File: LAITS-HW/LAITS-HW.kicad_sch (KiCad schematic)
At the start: 0 parts

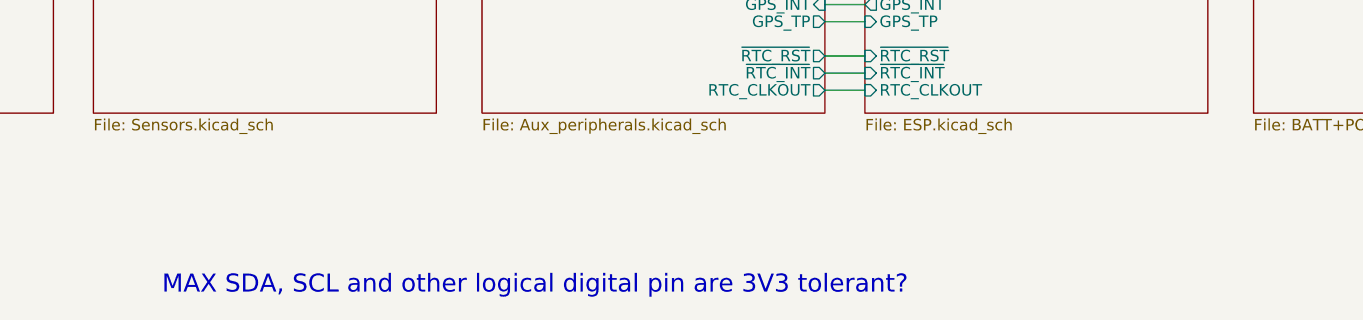
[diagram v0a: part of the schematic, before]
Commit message: improved silkscreen placement and some minor changes
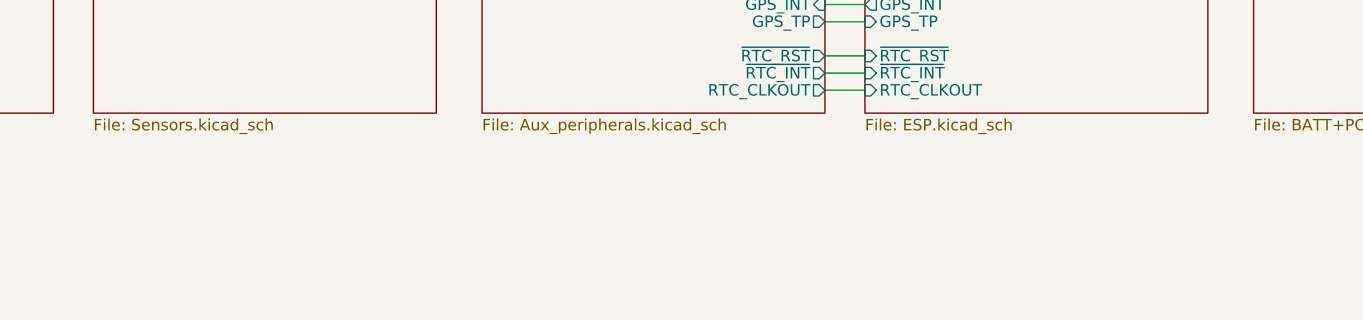
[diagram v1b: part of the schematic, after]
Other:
- note removed: "MAX SDA, SCL and other logical digital pin are 3V3 tolerant?"
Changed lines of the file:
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@@
     )
-  )
-  (text "MAX SDA, SCL and other logical digital pin are 3V3 tolerant?"
-    (at 95.885 141.605 0)
-    (effects (font (size 2 2)) (justify left bottom))
   )
   (sheet (at 131.445 69.85) (size 38.1 51.435) (fields_autoplaced)

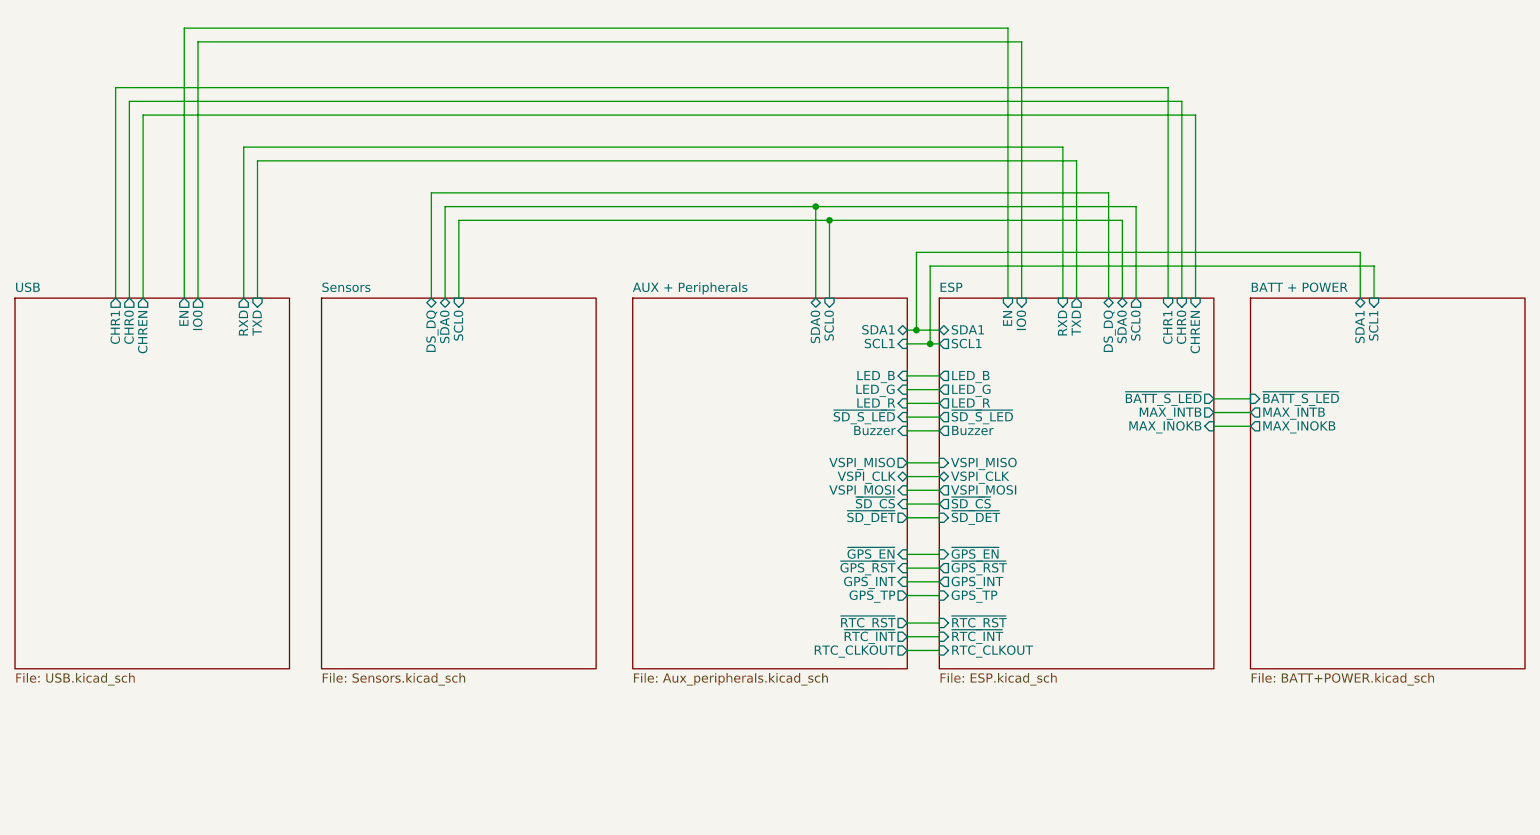
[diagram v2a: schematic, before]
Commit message: Fixed a minor bug in the assignment of SDA0 and SCL0 pins, doesn't affect Hardware, swap in firmware
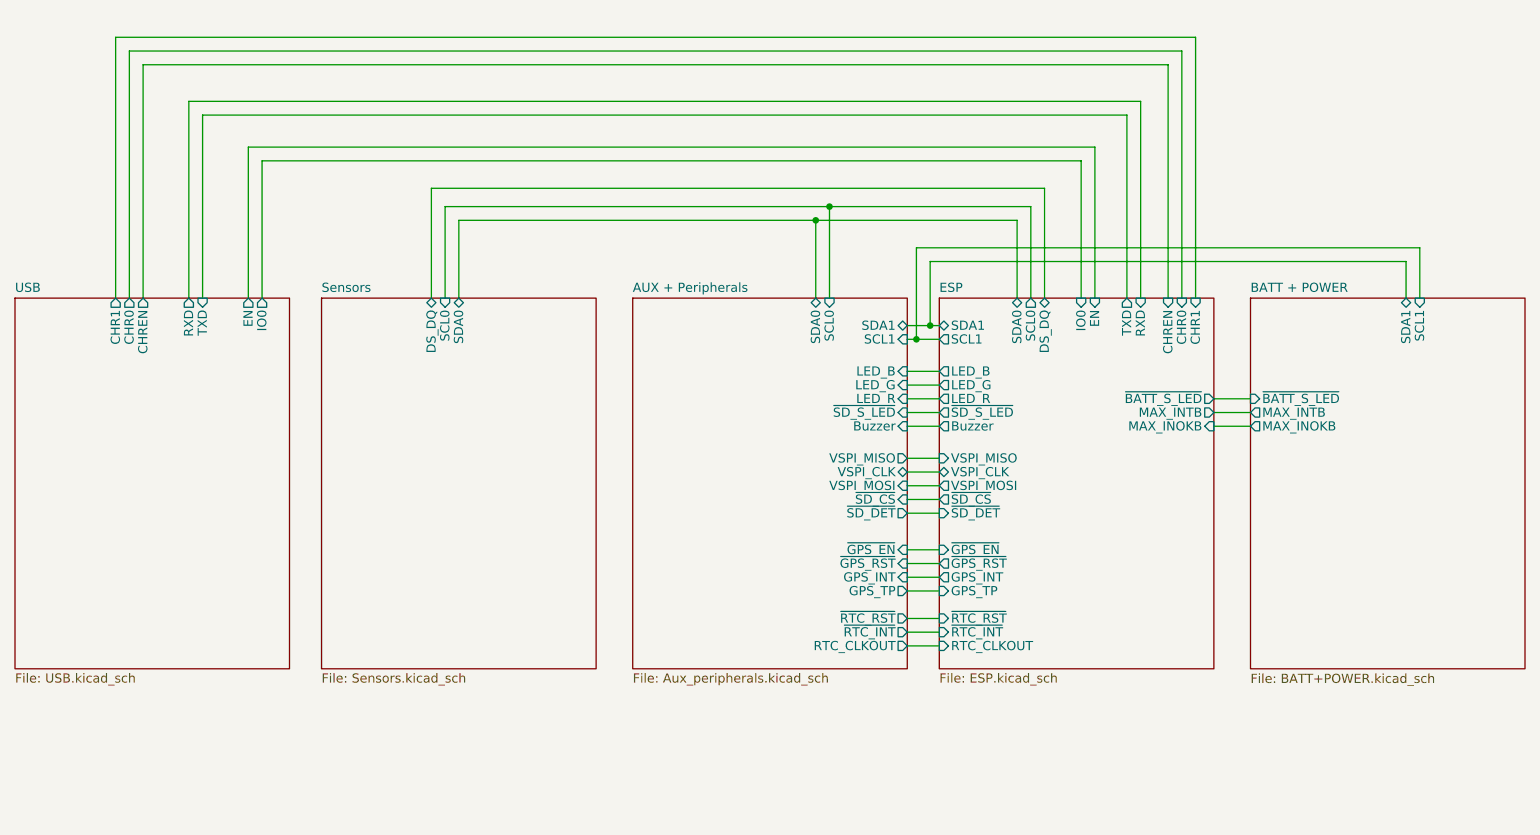
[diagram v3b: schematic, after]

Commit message: Now LAITS notify charge state also when turned off
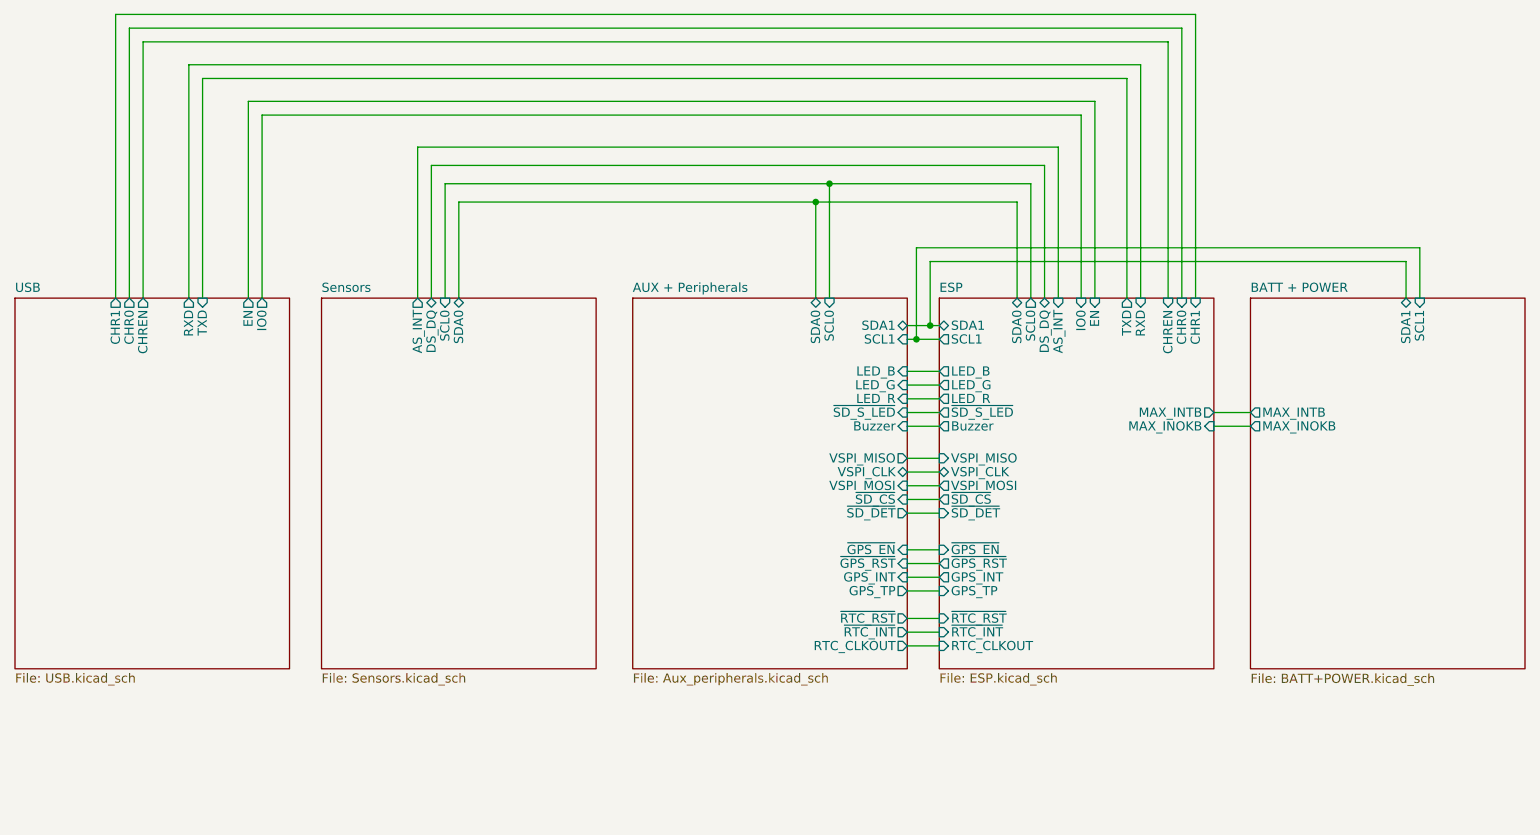
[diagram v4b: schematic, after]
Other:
- sheet BATT + POWER ports: added none; removed ~{BATT_S_LED}
- sheet ESP ports: added AS_INT; removed ~{BATT_S_LED}
- sheet Sensors ports: added AS_INT; removed none
